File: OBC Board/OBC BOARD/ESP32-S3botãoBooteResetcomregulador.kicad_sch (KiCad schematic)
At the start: 11 parts, among them SW1 SW_Push_Dual, SW2 SW_Push_Dual, U1 AMS1117

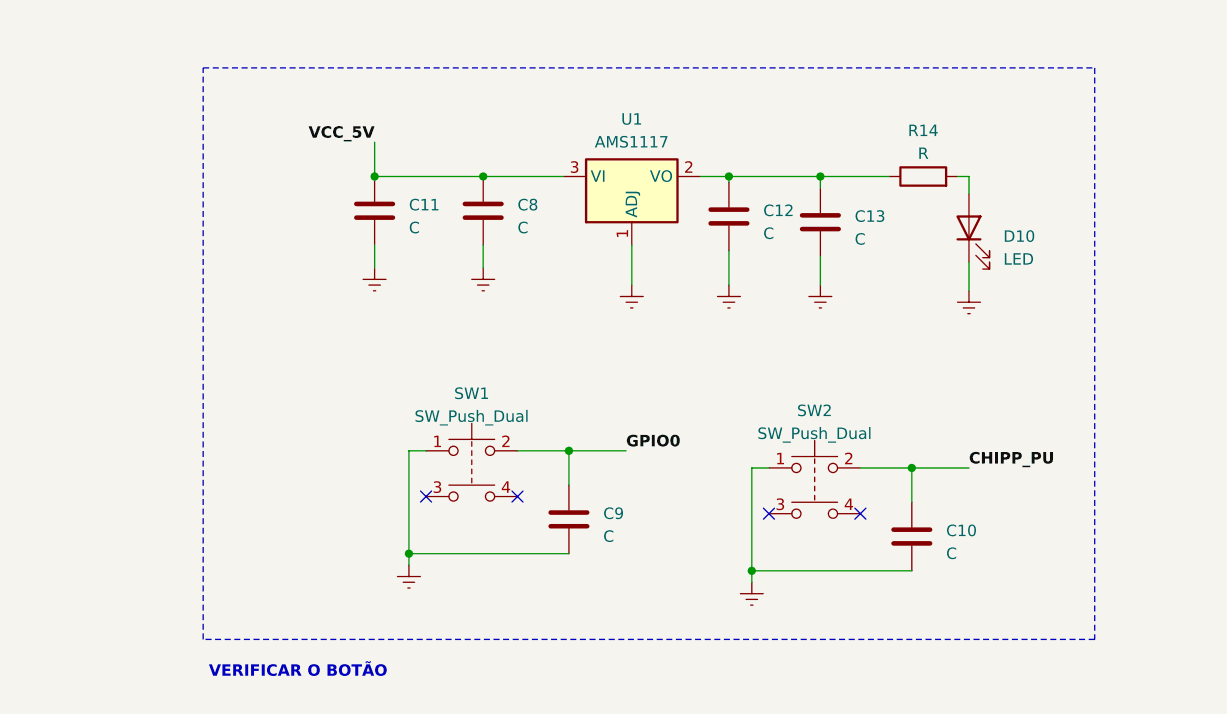
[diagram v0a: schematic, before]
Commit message: Realização do diagrama de blocos, test points, padronização e mudança dos caminhos das bibliotecas de footprints e simbolos
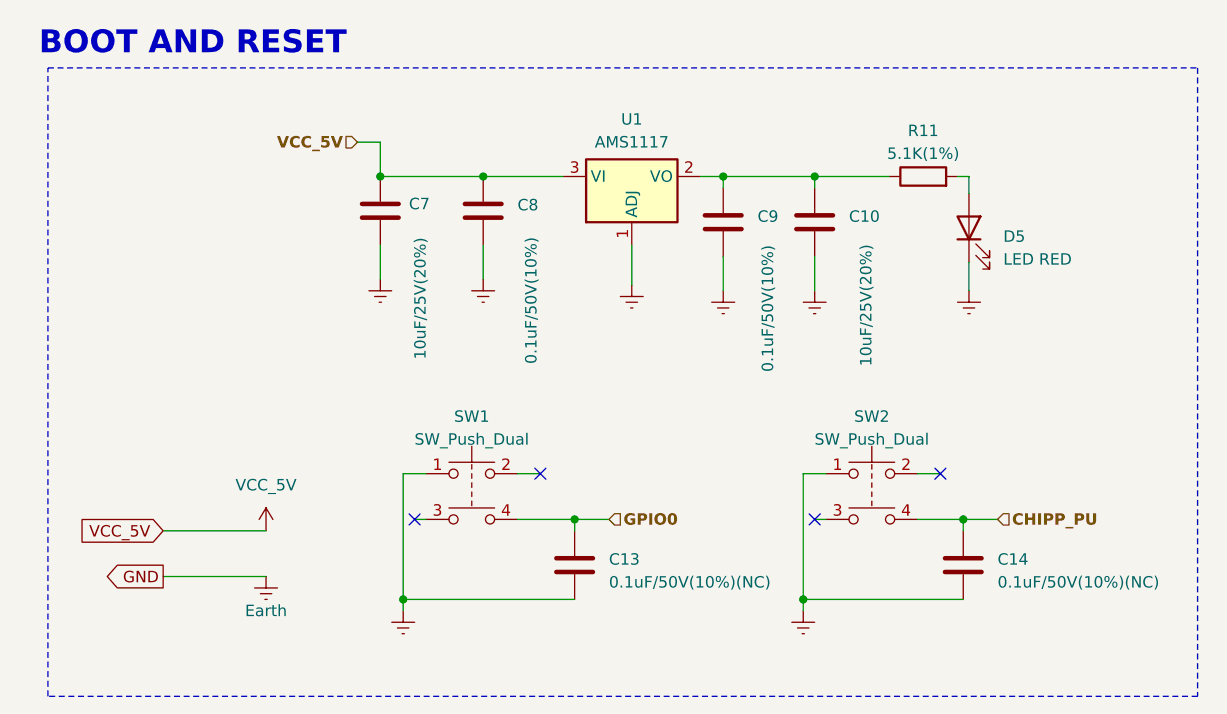
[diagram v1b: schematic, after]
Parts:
- C10: renamed from C13; value C -> 10uF/25V(20%); footprint (none) -> Capacitor_SMD:C_0402_1005Metric
- C13: renamed from C9; value C -> 0.1uF/50V(10%)(NC); footprint (none) -> Capacitor_SMD:C_0402_1005Metric
- C14: renamed from C10; value C -> 0.1uF/50V(10%)(NC); footprint (none) -> Capacitor_SMD:C_0402_1005Metric
- C7: renamed from C11; value C -> 10uF/25V(20%); footprint (none) -> Capacitor_SMD:C_0402_1005Metric
- C8: value C -> 0.1uF/50V(10%); footprint (none) -> Capacitor_SMD:C_0402_1005Metric
- C9: renamed from C12; value C -> 0.1uF/50V(10%); footprint (none) -> Capacitor_SMD:C_0402_1005Metric
- D5: renamed from D10; value LED -> LED RED; footprint (none) -> LED_SMD:LED_PLCC-2_3.4x3.0mm_AK
- R11: renamed from R14; value R -> 5.1K(1%); footprint (none) -> Resistor_SMD:R_0603_1608Metric
- SW1, SW2: footprint (none) -> Button_Switch_THT:SW_PUSH_6mm_H4.3mm
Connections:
- net CHIPP_PU: now also SW2.4; no longer SW2.2
- net GPIO0: now also SW1.4; no longer SW1.2
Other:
- note added: "BOOT AND RESET"
- note removed: "VERIFICAR O BOTÃO"
- title: ICARUS-2 OBCH -> ICARUS-2 OBDH
- moved on the sheet: C10, C13, C14, C7, C9, SW1, SW2

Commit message: Junção dos projetos FPGA e ESP32. Biblioteca de simbolos e footprints realizadas. Definição do caminho para os arquivos. Inclusão do esquema librecube.
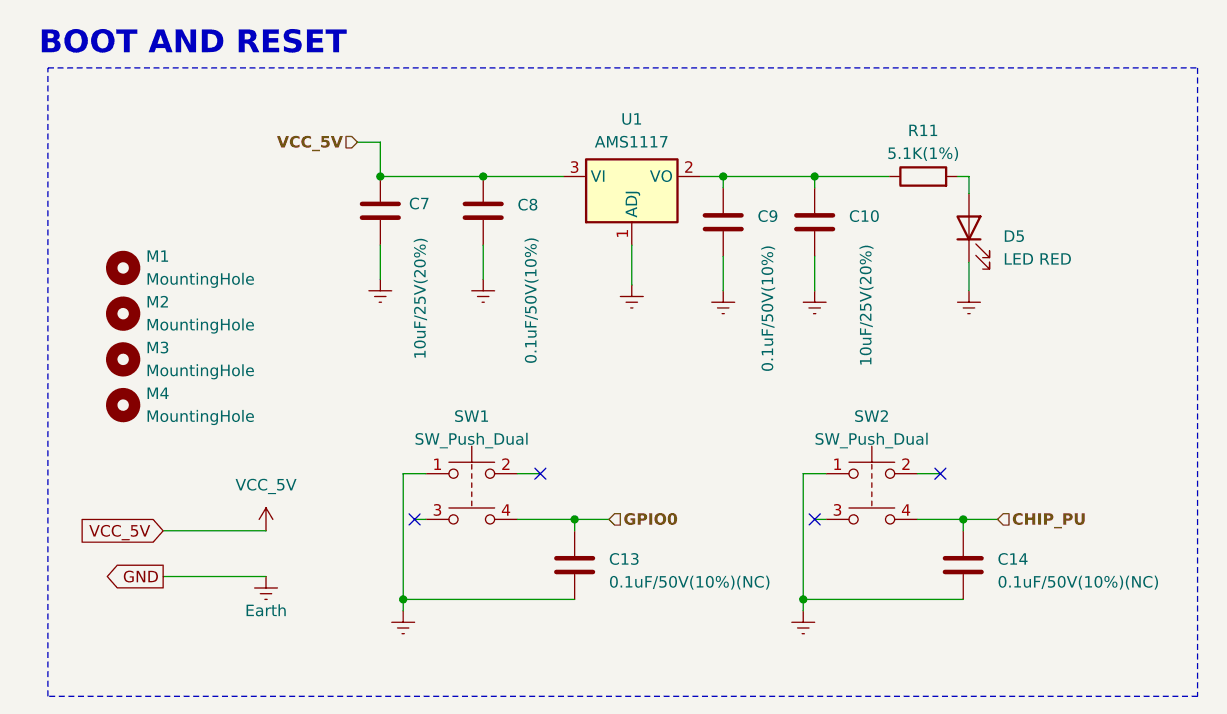
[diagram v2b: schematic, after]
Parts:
- added M1, M2, M3, M4: MountingHole, MountingHole:MountingHole_3.2mm_M3_Pad, symbol Mechanical:MountingHole
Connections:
- net CHIPP_PU renamed CHIP_PU
